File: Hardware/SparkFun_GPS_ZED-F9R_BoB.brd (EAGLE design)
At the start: 43.2 x 50.8 mm, 140 parts, among them J1 U.FL, J3 QWIIC_RIGHT_ANGLE, J4 QWIIC_RIGHT_ANGLE, U1 DUAL-OPTO_HCPL-073L, U2 U-BLOX_ZED_F9R, U3 UHS_INVERTER_SCHMITT_TRIGGERS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, U4 UHS_INVERTER_SCHMITT_TRIGGERS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, U5 3.3V

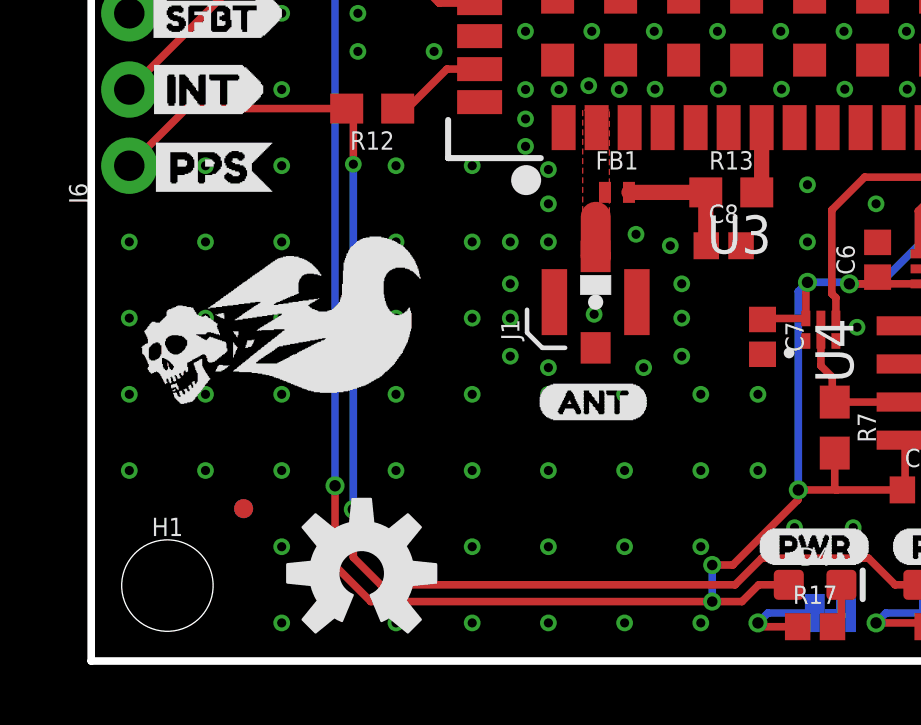
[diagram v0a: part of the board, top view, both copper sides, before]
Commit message: Adds silk for 3 axes and repanelizes
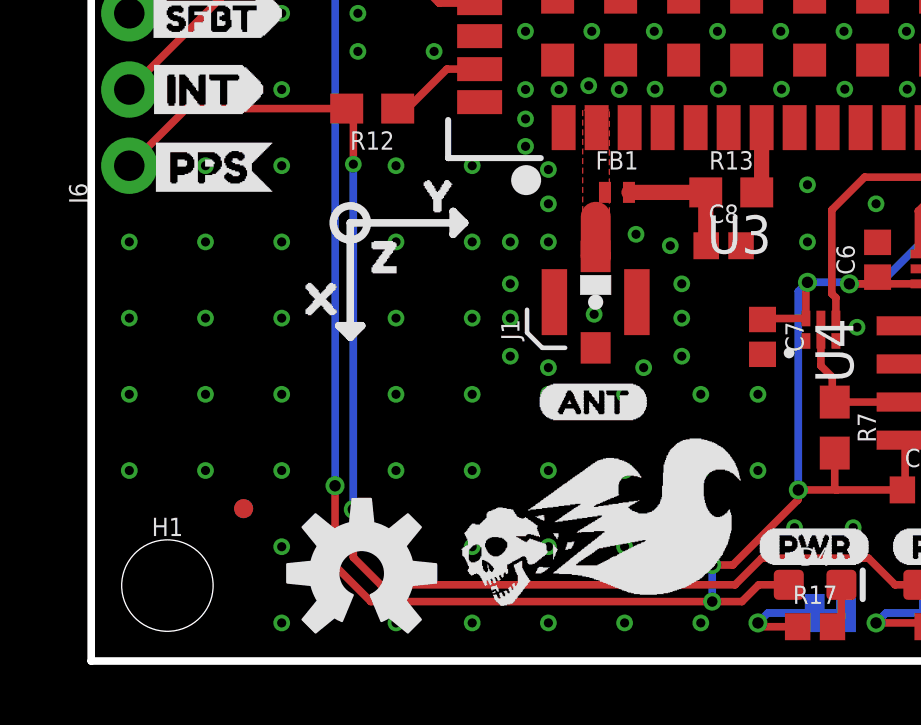
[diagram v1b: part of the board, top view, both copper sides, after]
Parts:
- added U$32: (no value), Orientation:X1
- added U$50, U$52: (no value), Orientation:Y2
- added U$57, U$63: (no value), Orientation:Z0
- moved U$20 12.6 mm to (17.0, 4.70)
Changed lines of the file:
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@@
 <text x="12.7" y="-6.35" size="1.778" layer="47" font="vector" ratio="15">Units In Inches</text>
 <text x="42.037" y="8.636" size="1.27" layer="16" font="vector" ratio="15" rot="SMR270">v10</text>
+<wire x1="8.636" y1="10.795" x2="8.636" y2="14.605" width="0.254" layer="21"/>
+<wire x1="8.636" y1="14.605" x2="12.446" y2="14.605" width="0.254" layer="21"/>
+<wire x1="8.636" y1="10.795" x2="8.255" y2="11.176" width="0.254" layer="21"/>
+<wire x1="8.255" y1="11.176" x2="9.017" y2="11.176" width="0.254" layer="21"/>
+<wire x1="9.017" y1="11.176" x2="8.636" y2="10.795" width="0.254" layer="21"/>
+<wire x1="12.446" y1="14.605" x2="12.065" y2="14.986" width="0.254" layer="21"/>
+<wire x1="12.065" y1="14.986" x2="12.065" y2="14.224" width="0.254" layer="21"/>
+<wire x1="12.065" y1="14.224" x2="12.446" y2="14.605" width="0.254" layer="21"/>
+<circle x="8.636" y="14.605" radius="0.567959375" width="0.254" layer="21"/>
+<wire x1="8.636" y1="10.795" x2="8.636" y2="14.605" width="0.254" layer="22"/>
+<wire x1="8.636" y1="14.605" x2="12.446" y2="14.605" width="0.254" layer="22"/>
+<wire x1="8.636" y1="10.795" x2="9.017" y2="11.176" width="0.254" layer="22"/>
+<wire x1="9.017" y1="11.176" x2="8.255" y2="11.176" width="0.254" layer="22"/>
+<wire x1="8.255" y1="11.176" x2="8.636" y2="10.795" width="0.254" layer="22"/>
+<wire x1="12.446" y1="14.605" x2="12.065" y2="14.986" width="0.254" layer="22"/>
+<wire x1="12.065" y1="14.986" x2="12.065" y2="14.224" width="0.254" layer="22"/>
+<wire x1="12.065" y1="14.224" x2="12.446" y2="14.605" width="0.254" layer="22"/>
+<wire x1="8.2005875" y1="15.040409375" x2="9.0986125" y2="14.142384375" width="0.254" layer="22"/>
+<wire x1="9.046009375" y1="14.989609375" x2="8.147984375" y2="14.091584375" width="0.254" layer="22"/>
 </plain>
 <attributes>
@@
 <element name="U$25" library="dead reckoning" package="GPS_DEAD_RECKONING0" value="" x="32.004" y="33.274" smashed="yes" rot="MR0"/>
 <element name="U$19" library="Dead#Reckoning#GPS#board#silk#FINAL#png" package="DEAD#RECKONING#GPS#BOARD#SILK#FINAL#JPG" value="" x="22.86" y="22.86" smashed="yes" rot="MR0"/>
-<element name="U$20" library="Dead#Reckoning#GPS#board#silk#FINALSMALL" package="DEAD#RECKONING#GPS#BOARD#SILK#FINAL#JPG" value="" x="6.35" y="11.43" smashed="yes"/>
+<element name="U$20" library="Dead#Reckoning#GPS#board#silk#FINALSMALL" package="DEAD#RECKONING#GPS#BOARD#SILK#FINAL#JPG" value="" x="17.018" y="4.699" smashed="yes"/>
+<element name="U$32" library="Orientation" package="X1" value="" x="6.223" y="12.065" smashed="yes"/>
+<element name="U$50" library="Orientation" package="Y2" value="" x="10.16" y="15.494" smashed="yes"/>
+<element name="U$52" library="Orientation" package="Y2" value="" x="12.954" y="15.494" smashed="yes" rot="MR0"/>
+<element name="U$57" library="Orientation" package="Z0" value="" x="11.176" y="13.462" smashed="yes" rot="MR0"/>
+<element name="U$63" library="Orientation" package="Z0" value="" x="8.382" y="13.462" smashed="yes"/>
 </elements>
 <signals>

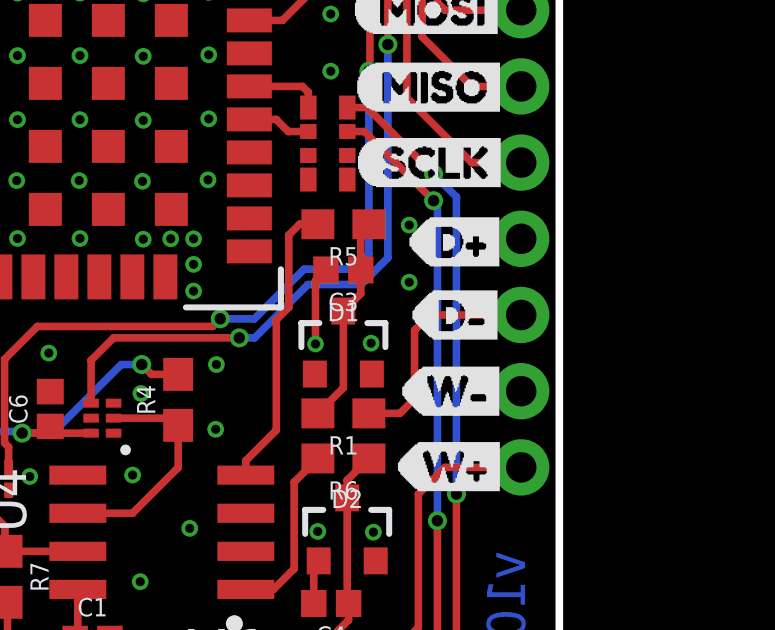
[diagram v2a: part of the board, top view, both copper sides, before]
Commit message: Fixes silk and repanelizes
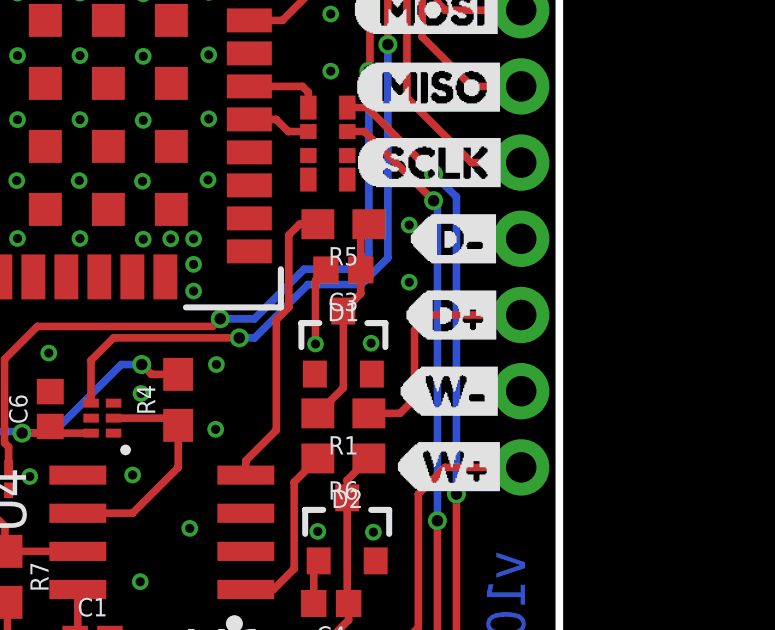
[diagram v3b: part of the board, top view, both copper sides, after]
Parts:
- U$60: device wt_dir:D#0 -> D+,D-:D#0
- U$61: device wt_dir:D#1 -> D+,D-:W#2
- U$64: device wt_dir:W#2 -> D+,D-:D#1
- U$65: device wt_dir:W#3 -> D+,D-:W#3
- moved U$64 8.52 mm to (41.5, 19.1), turned to 0 degrees
- moved U$61 6.14 mm to (41.7, 11.4), turned to 0 degrees
- moved U$60 4.19 mm to (41.5, 16.5), turned to 0 degrees
- moved U$65 3.83 mm to (41.7, 14.0), turned to 0 degrees
- moved U$6 2.54 mm to (38.2, 19.1)
- moved U$3 2.44 mm to (38.0, 16.5)
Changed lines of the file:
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@@
 <?xml version="1.0" encoding="utf-8"?>
 <!DOCTYPE eagle SYSTEM "eagle.dtd">
-<eagle version="9.5.2">
+<eagle version="9.5.1">
 <drawing>
 <settings>
@@
 <setting verticaltext="up"/>
 </settings>
-<grid distance="0.05" unitdist="inch" unit="inch" style="lines" multiple="1" display="yes" altdistance="0.005" altunitdist="inch" altunit="inch"/>
+<grid distance="0.05" unitdist="inch" unit="inch" style="lines" multiple="1" display="yes" altdistance="0.05" altunitdist="mm" altunit="mm"/>
 <layers>
 <layer number="1" name="Top" color="4" fill="1" visible="yes" active="yes"/>
@@
 <layer number="23" name="tOrigins" color="15" fill="1" visible="yes" active="yes"/>
 <layer number="24" name="bOrigins" color="15" fill="1" visible="yes" active="yes"/>
-<layer number="25" name="tNames" color="7" fill="1" visible="no" active="yes"/>
-<layer number="26" name="bNames" color="7" fill="1" visible="no" active="yes"/>
-<layer number="27" name="tValues" color="7" fill="1" visible="no" active="yes"/>
-<layer number="28" name="bValues" color="7" fill="1" visible="no" active="yes"/>
-<layer number="29" name="tStop" color="7" fill="3" visible="no" active="yes"/>
-<layer number="30" name="bStop" color="7" fill="6" visible="no" active="yes"/>
-<layer number="31" name="tCream" color="7" fill="4" visible="no" active="yes"/>
-<layer number="32" name="bCream" color="7" fill="5" visible="no" active="yes"/>
-<layer number="33" name="tFinish" color="6" fill="3" visible="no" active="yes"/>
-<layer number="34" name="bFinish" color="6" fill="6" visible="no" active="yes"/>
-<layer number="35" name="tGlue" color="7" fill="4" visible="no" active="yes"/>
-<layer number="36" name="bGlue" color="7" fill="5" visible="no" active="yes"/>
-<layer number="37" name="tTest" color="7" fill="1" visible="no" active="yes"/>
-<layer number="38" name="bTest" color="7" fill="1" visible="no" active="yes"/>
-<layer number="39" name="tKeepout" color="4" fill="11" visible="no" active="yes"/>
-<layer number="40" name="bKeepout" color="1" fill="11" visible="no" active="yes"/>
-<layer number="41" name="tRestrict" color="4" fill="10" visible="no" active="yes"/>
-<layer number="42" name="bRestrict" color="1" fill="10" visible="no" active="yes"/>
-<layer number="43" name="vRestrict" color="2" fill="10" visible="no" active="yes"/>
-<layer number="44" name="Drills" color="7" fill="1" visible="no" active="yes"/>
+<layer number="25" name="tNames" color="7" fill="1" visible="yes" active="yes"/>
+<layer number="26" name="bNames" color="7" fill="1" visible="yes" active="yes"/>
+<layer number="27" name="tValues" color="7" fill="1" visible="yes" active="yes"/>
+<layer number="28" name="bValues" color="7" fill="1" visible="yes" active="yes"/>
+<layer number="29" name="tStop" color="7" fill="3" visible="yes" active="yes"/>
+<layer number="30" name="bStop" color="7" fill="6" visible="yes" active="yes"/>
+<layer number="31" name="tCream" color="7" fill="4" visible="yes" active="yes"/>
+<layer number="32" name="bCream" color="7" fill="5" visible="yes" active="yes"/>
+<layer number="33" name="tFinish" color="6" fill="3" visible="yes" active="yes"/>
+<layer number="34" name="bFinish" color="6" fill="6" visible="yes" active="yes"/>
+<layer number="35" name="tGlue" color="7" fill="4" visible="yes" active="yes"/>
+<layer number="36" name="bGlue" color="7" fill="5" visible="yes" active="yes"/>
+<layer number="37" name="tTest" color="7" fill="1" visible="yes" active="yes"/>
+<layer number="38" name="bTest" color="7" fill="1" visible="yes" active="yes"/>
+<layer number="39" name="tKeepout" color="4" fill="11" visible="yes" active="yes"/>
+<layer number="40" name="bKeepout" color="1" fill="11" visible="yes" active="yes"/>
+<layer number="41" name="tRestrict" color="4" fill="10" visible="yes" active="yes"/>
+<layer number="42" name="bRestrict" color="1" fill="10" visible="yes" active="yes"/>
+<layer number="43" name="vRestrict" color="2" fill="10" visible="yes" active="yes"/>
+<layer number="44" name="Drills" color="7" fill="1" visible="yes" active="yes"/>
 <layer number="45" name="Holes" color="7" fill="1" visible="yes" active="yes"/>
-<layer number="46" name="Milling" color="3" fill="1" visible="no" active="yes"/>
-<layer number="47" name="Measures" color="7" fill="1" visible="no" active="yes"/>
-<layer number="48" name="Document" color="7" fill="1" visible="no" active="yes"/>
+<layer number="46" name="Milling" color="3" fill="1" visible="yes" active="yes"/>
+<layer number="47" name="Measures" color="7" fill="1" visible="yes" active="yes"/>
+<layer number="48" name="Document" color="7" fill="1" visible="yes" active="yes"/>
 <layer number="49" name="Reference" color="13" fill="1" visible="yes" active="yes"/>
-<layer number="50" name="dxf" color="7" fill="1" visible="no" active="yes"/>
+<layer number="50" name="dxf" color="7" fill="1" visible="yes" active="yes"/>
 <layer number="51" name="tDocu" color="6" fill="1" visible="yes" active="yes"/>
-<layer number="52" name="bDocu" color="7" fill="1" visible="no" active="yes"/>
+<layer number="52" name="bDocu" color="7" fill="1" visible="yes" active="yes"/>
 <layer number="53" name="tGND_GNDA" color="7" fill="9" visible="no" active="no"/>
 <layer number="54" name="bGND_GNDA" color="1" fill="9" visible="no" active="no"/>
@@
 <layer number="115" name="ReferenceISLANDS" color="7" fill="1" visible="no" active="no"/>
 <layer number="116" name="Patch_BOT" color="9" fill="4" visible="no" active="no"/>
-<layer number="117" name="PM_Ref" color="26" fill="1" visible="no" active="yes"/>
+<layer number="117" name="PM_Ref" color="26" fill="1" visible="yes" active="yes"/>
 <layer number="118" name="Rect_Pads" color="7" fill="1" visible="no" active="no"/>
-<layer number="119" name="PF_Ref" color="31" fill="1" visible="no" active="yes"/>
-<layer number="120" name="WFL_Ref" color="25" fill="1" visible="no" active="yes"/>
+<layer number="119" name="PF_Ref" color="31" fill="1" visible="yes" active="yes"/>
+<layer number="120" name="WFL_Ref" color="25" fill="1" visible="yes" active="yes"/>
 <layer number="121" name="_tsilk" color="7" fill="1" visible="no" active="no"/>
 <layer number="122" name="_bsilk" color="7" fill="1" visible="no" active="no"/>
@@
 <attribute name="VALUE" x="21.6152" y="10.8048" size="0.6096" layer="27" font="vector" ratio="20" rot="R270" align="top-center"/>
 </element>
-<element name="U$60" library="wt_dir" package="D#0" value="" x="38.1" y="18.923" smashed="yes" rot="MR180"/>
-<element name="U$61" library="wt_dir" package="D#1" value="" x="38.227" y="16.51" smashed="yes" rot="MR180"/>
-<element name="U$64" library="wt_dir" package="W#2" value="" x="37.719" y="11.43" smashed="yes" rot="MR180"/>
-<element name="U$65" library="wt_dir" package="W#3" value="" x="37.846" y="13.97" smashed="yes" rot="MR180"/>
 <element name="C5" library="SparkFun-Capacitors" package="0603" value="1.0uF" x="19.7866" y="34.7726" smashed="yes">
 <attribute name="NAME" x="19.7866" y="35.5346" size="0.6096" layer="25" font="vector" ratio="20" align="bottom-center"/>
@@
 <element name="U$66" library="Labels" package="MISO-(]-04" value="" x="36.322" y="24.1046" smashed="yes"/>
 <element name="U$69" library="Labels" package="MOSI-(]-04" value="" x="36.2458" y="26.6954" smashed="yes"/>
-<element name="U$3" library="wt_dir" package="D#0" value="" x="38.1" y="18.9484" smashed="yes"/>
-<element name="U$6" library="wt_dir" package="D#1" value="" x="38.2016" y="16.51" smashed="yes"/>
+<element name="U$3" library="wt_dir" package="D#0" value="" x="38" y="16.5084" smashed="yes"/>
+<element name="U$6" library="wt_dir" package="D#1" value="" x="38.1516" y="19.05" smashed="yes"/>
 <element name="U$9" library="wt_dir" package="W#2" value="" x="37.719" y="11.4554" smashed="yes"/>
-<element name="U$10" library="wt_dir" package="W#3" value="" x="37.8206" y="13.97" smashed="yes"/>
+<element name="U$10" library="wt_dir" package="W#3" value="" x="37.7706" y="13.97" smashed="yes"/>
 <element name="U$11" library="Labels" package="5V" value="" x="37.9476" y="34.29" smashed="yes"/>
 <element name="U$12" library="ALL_LABELS" package="INT1" value="" x="1.5748" y="19.05" smashed="yes"/>
@@
 <element name="U$57" library="Orientation" package="Z0" value="" x="11.176" y="13.462" smashed="yes" rot="MR0"/>
 <element name="U$63" library="Orientation" package="Z0" value="" x="8.382" y="13.462" smashed="yes"/>
+<element name="U$60" library="D+,D-" package="D#0" value="" x="41.529" y="16.51" smashed="yes" rot="MR0"/>
+<element name="U$61" library="D+,D-" package="W#2" value="" x="41.679" y="11.43" smashed="yes" rot="MR0"/>
+<element name="U$64" library="D+,D-" package="D#1" value="" x="41.529" y="19.05" smashed="yes" rot="MR0"/>
+<element name="U$65" library="D+,D-" package="W#3" value="" x="41.679" y="13.97" smashed="yes" rot="MR0"/>
 </elements>
 <signals>
